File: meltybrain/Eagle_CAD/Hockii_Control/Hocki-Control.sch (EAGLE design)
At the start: 77 parts, among them CN1 JST_2PIN, J1 SM03B-SRSS-TB(LF)(SN), J2 SM04B-SRSS-TB(LF)(SN), J4 SM04B-SRSS-TB(LF)(SN), J7 SM02B-SRSS-TB(LF)(SN), J8 SM02B-SRSS-TB(LF)(SN), U1 AP63200, U13 TMP235A4DCKR, U14 ADXL375, U15 NL27WZ32USG, U16 ADXL375, U17 ADXL375, U18 NL27WZ32USG, U19 ADXL375, U2 TEENSY_4.1, U3 AP2210K-5.0TRG1, U4 AP2210K-3.3TRG1, U5 TXS0104ED, U6 LDL212PU50R, U7 LIS3MDLTR

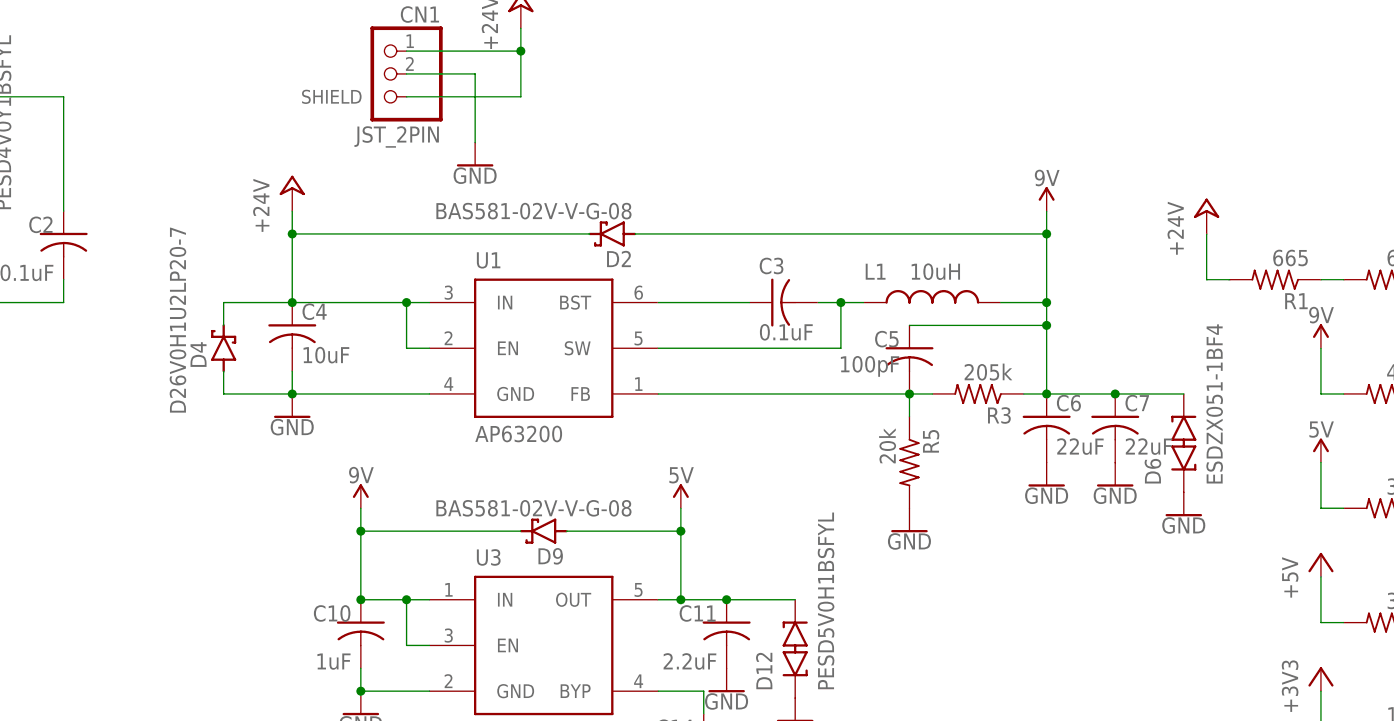
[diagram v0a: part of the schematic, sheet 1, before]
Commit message: add replacement 9V regulator to schematic
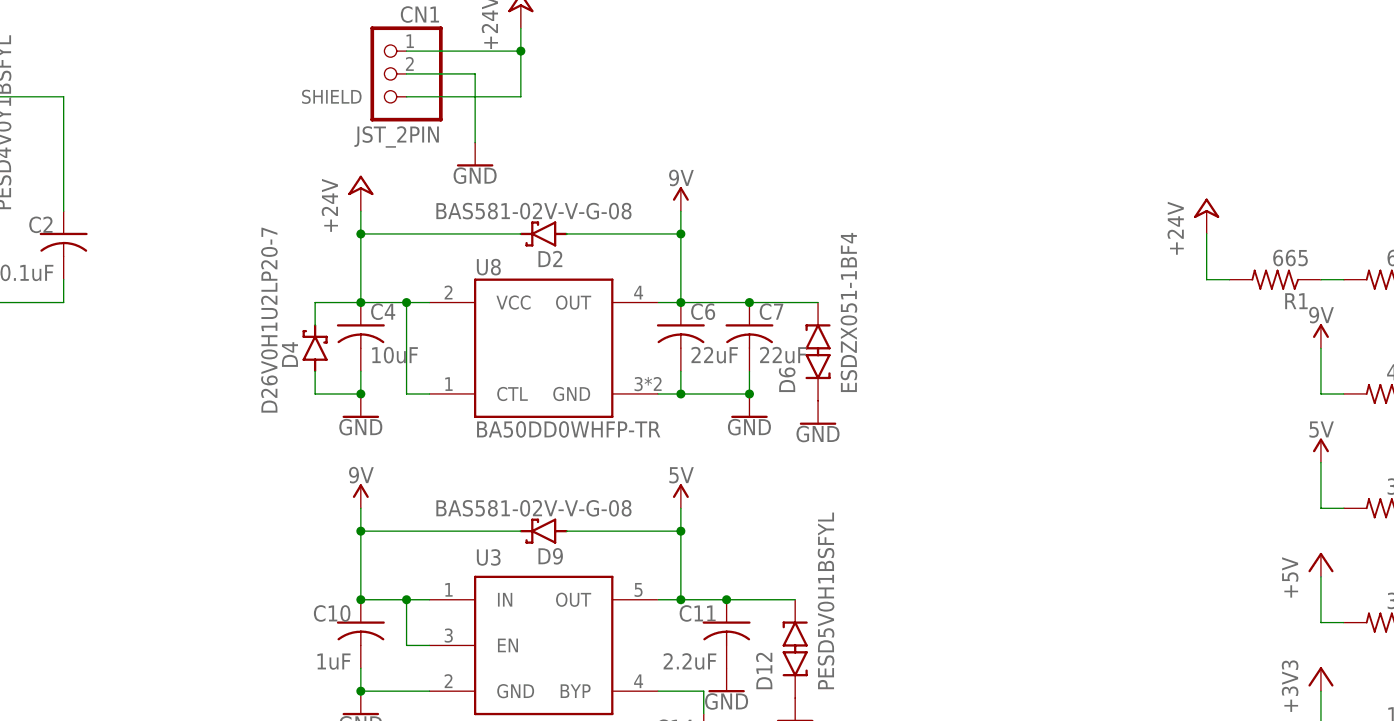
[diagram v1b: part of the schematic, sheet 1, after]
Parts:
- removed C3: 0.1uF, rcl:C-USC0603
- removed C5: 100pF, rcl:C-USC0603
- removed L1: 10uH, Hocki_Library:LQH5BPN100M38L
- removed R3: 205k, rcl:R-US_R0603
- removed R5: 20k, rcl:R-US_R0603
- removed U1: AP63200, Hocki_Library:AP63200
- added U8: BA50DD0WHFP-TR, Hocki_Library:BA50DD0WHFP-TR
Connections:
- removed net N$1: C3.1, U1.BST
- removed net N$12: C5.2, R3.2, R5.1, U1.FB
- removed net N$3: C3.2, L1.1, U1.SW
- net +24V: now also U8.CTL, U8.VCC; no longer U1.EN, U1.IN
- net 9V: now also U8.OUT; no longer C5.1, L1.2, R3.1
- net GND: now also U8.GND; no longer R5.2, U1.GND
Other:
- moved on the sheet: C4, C6, C7, D2, D4, D6

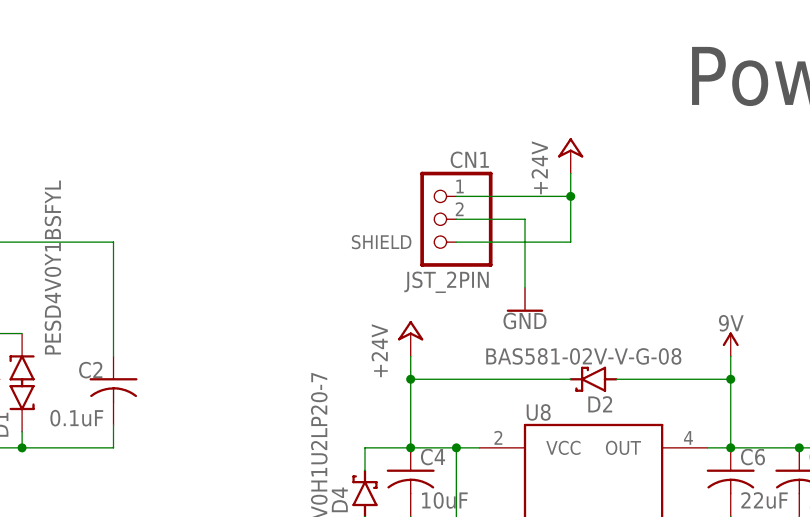
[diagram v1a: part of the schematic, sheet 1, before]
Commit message: swap power connector
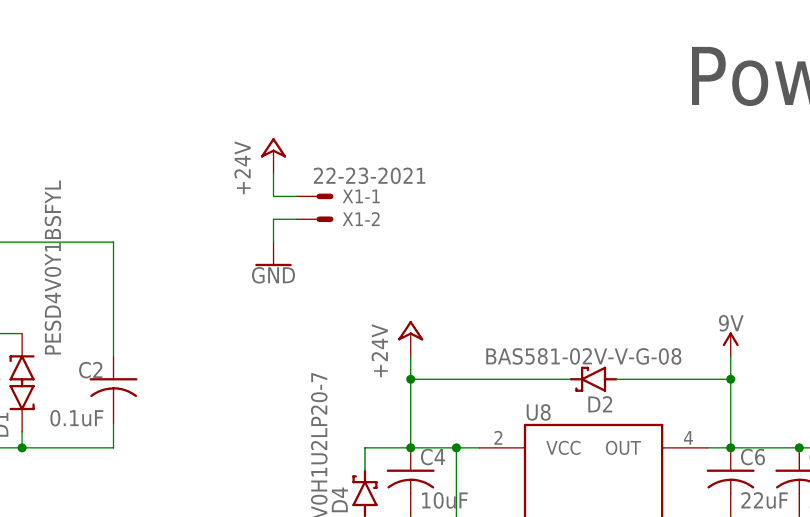
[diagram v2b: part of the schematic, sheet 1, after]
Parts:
- removed CN1: JST_2PIN, Hocki_Library:JST_2PIN
- added X1: 22-23-2021, con-molex:22-23-2021
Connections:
- net +24V: now also X1-1.S; no longer CN1.1, CN1.SHIELD
- net GND: now also X1-2.S; no longer CN1.2
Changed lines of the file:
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@@
 <part name="P+5" library="supply1" library_urn="urn:adsk.eagle:library:371" deviceset="+24V" device=""/>
 <part name="GND67" library="SparkFun-PowerSymbols" deviceset="GND" device=""/>
-<part name="CN1" library="Hocki_Library" deviceset="JST_2PIN" device="" package3d_urn="urn:adsk.eagle:package:22261884/2"/>
 <part name="D4" library="Hocki_Library" deviceset="D26V0H1U2LP20-7" device=""/>
 <part name="FRAME1" library="RoboJackets-Frames" deviceset="FRAME_11_17" device="">
@@
 <part name="GND6" library="SparkFun-PowerSymbols" deviceset="GND" device=""/>
 <part name="U8" library="Hocki_Library" deviceset="BA50DD0WHFP-TR" device=""/>
+<part name="X1" library="con-molex" library_urn="urn:adsk.eagle:library:165" deviceset="22-23-2021" device="" package3d_urn="urn:adsk.eagle:package:8078633/1"/>
 </parts>
 <sheets>
@@
 <attribute name="VALUE" x="187.96" y="22.606" size="1.778" layer="96" align="top-center"/>
 </instance>
-<instance part="P+5" gate="1" x="261.62" y="251.46" smashed="yes">
-<attribute name="VALUE" x="259.08" y="246.38" size="1.778" layer="96" rot="R90"/>
-</instance>
-<instance part="GND67" gate="1" x="256.54" y="233.68" smashed="yes">
-<attribute name="VALUE" x="256.54" y="233.426" size="1.778" layer="96" align="top-center"/>
-</instance>
-<instance part="CN1" gate="G$1" x="246.38" y="243.84" smashed="yes" rot="MR0">
-<attribute name="NAME" x="252.73" y="249.555" size="1.778" layer="95" rot="MR0"/>
-<attribute name="VALUE" x="252.73" y="236.22" size="1.778" layer="96" rot="MR0"/>
+<instance part="P+5" gate="1" x="228.6" y="251.46" smashed="yes">
+<attribute name="VALUE" x="226.06" y="246.38" size="1.778" layer="96" rot="R90"/>
+</instance>
+<instance part="GND67" gate="1" x="228.6" y="238.76" smashed="yes">
+<attribute name="VALUE" x="228.6" y="238.506" size="1.778" layer="96" align="top-center"/>
 </instance>
 <instance part="D4" gate="G$1" x="238.76" y="213.36" smashed="yes" rot="R90">
@@
 <attribute name="NAME" x="256.54" y="221.488" size="1.778" layer="95"/>
 <attribute name="VALUE" x="256.54" y="205.232" size="1.778" layer="96" align="top-left"/>
+</instance>
+<instance part="X1" gate="-1" x="233.68" y="246.38" smashed="yes">
+<attribute name="NAME" x="236.22" y="245.618" size="1.524" layer="95"/>
+<attribute name="VALUE" x="232.918" y="247.777" size="1.778" layer="96"/>
+</instance>
+<instance part="X1" gate="-2" x="233.68" y="243.84" smashed="yes">
+<attribute name="NAME" x="236.22" y="243.078" size="1.524" layer="95"/>
 </instance>
 </instances>
@@
 </segment>
 <segment>
-<pinref part="CN1" gate="G$1" pin="2"/>
-<wire x1="248.92" y1="243.84" x2="256.54" y2="243.84" width="0.1524" layer="91"/>
 <pinref part="GND67" gate="1" pin="GND"/>
-<wire x1="256.54" y1="243.84" x2="256.54" y2="236.22" width="0.1524" layer="91"/>
+<wire x1="228.6" y1="243.84" x2="228.6" y2="241.3" width="0.1524" layer="91"/>
+<pinref part="X1" gate="-2" pin="S"/>
+<wire x1="231.14" y1="243.84" x2="228.6" y2="243.84" width="0.1524" layer="91"/>
 </segment>
 <segment>
@@
 </segment>
 <segment>
-<pinref part="CN1" gate="G$1" pin="SHIELD"/>
-<wire x1="248.92" y1="241.3" x2="261.62" y2="241.3" width="0.1524" layer="91"/>
 <pinref part="P+5" gate="1" pin="+24V"/>
-<pinref part="CN1" gate="G$1" pin="1"/>
-<wire x1="261.62" y1="241.3" x2="261.62" y2="246.38" width="0.1524" layer="91"/>
-<wire x1="261.62" y1="246.38" x2="261.62" y2="248.92" width="0.1524" layer="91"/>
-<wire x1="248.92" y1="246.38" x2="261.62" y2="246.38" width="0.1524" layer="91"/>
-<junction x="261.62" y="246.38"/>
-</segment>
-<segment>
+<wire x1="228.6" y1="246.38" x2="228.6" y2="248.92" width="0.1524" layer="91"/>
+<pinref part="X1" gate="-1" pin="S"/>
+<wire x1="231.14" y1="246.38" x2="228.6" y2="246.38" width="0.1524" layer="91"/>
+</segment>
+<segment>

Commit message: order Hockii v1
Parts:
- removed C12: 1uF, rcl:C-USC0603
- removed C13: 2.2uF, rcl:C-USC0603
- removed C15: 100pF, rcl:C-USC0603
- removed D10: BAS581-02V-V-G-08, Hocki_Library:BAS581-02V-V-G-08
- removed D11: GREEN, SparkFun-LED:LED-GREEN0603
- removed D13: PESD4V0Y1BSFYL, Hocki_Library:PESD4V0Y1BSFYL
- removed FB1: MPZ1608R391ATD25, Hocki_Library:MPZ1608R391ATD25
- removed R10: 169, rcl:R-US_R0603
- removed U4: AP2210K-3.3TRG1, Hocki_Library:AP2210K-3.3TRG1
- added C3: 0.1uF, rcl:C-USC0603
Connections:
- removed net +3V3: D10.A, FB1.2, R10.2
- removed net N$11: C15.1, U4.BYP
- removed net N$17: D11.A, R10.1
- removed net N$28: C13.1, D13.C2, FB1.1, U4.OUT
- net 3.3V: now also C3.1
- net 5V: no longer C12.1, D10.C, U4.EN, U4.IN
- net GND: now also C3.2; no longer C12.2, C13.2, C15.2, D11.C, D13.C1, U4.GND
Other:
- moved on the sheet: C19, C20, D14, R11
